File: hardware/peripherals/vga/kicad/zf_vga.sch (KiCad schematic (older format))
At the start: 33 parts

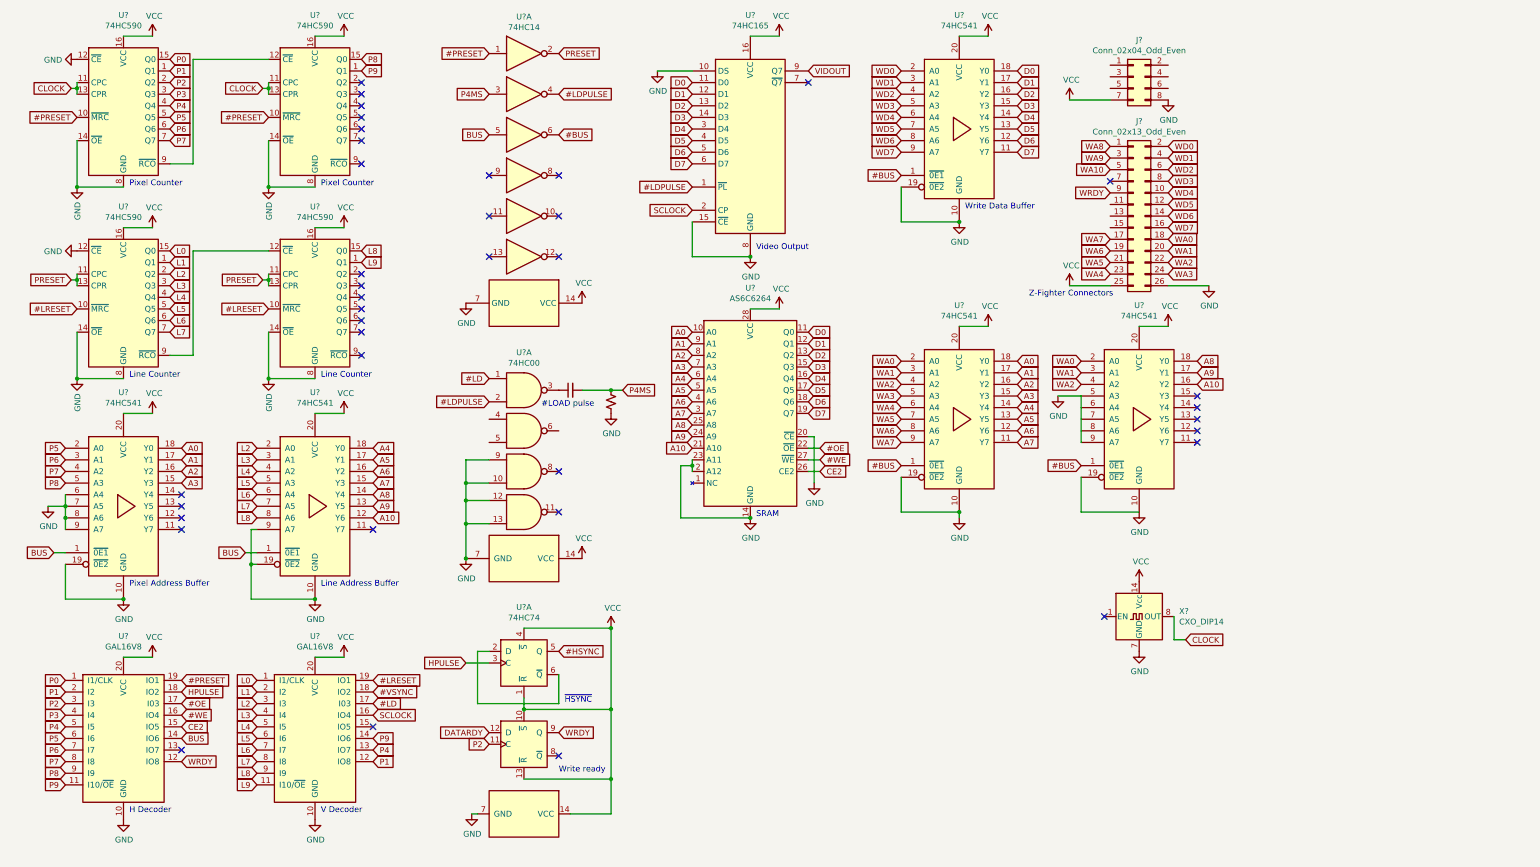
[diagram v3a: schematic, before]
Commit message: 4040 counter ICs
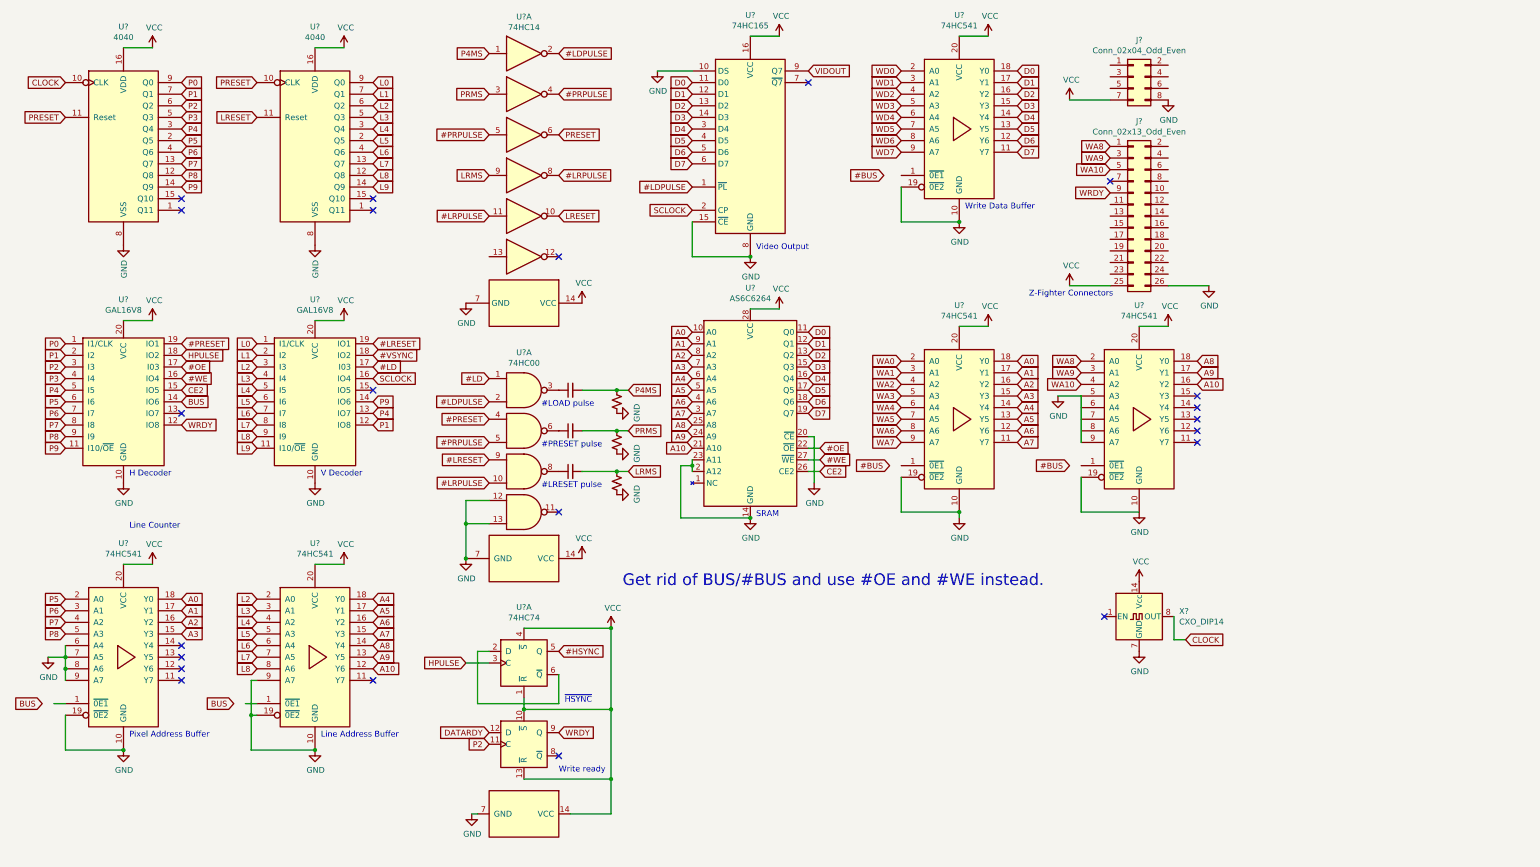
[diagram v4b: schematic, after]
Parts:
- removed U? (x4): 74HC590, symbol 74xx:74HC590
- added C? (x2): C_Small, symbol Device:C_Small
- added R? (x2): R_Small_US, symbol Device:R_Small_US
- added U? (x2): 4040, symbol 4xxx:4040
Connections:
- net #BUS: no longer U?.1 (~0E1), U?.1 (~0E1), U?.1 (~0E1), U?.6
- net #LDPULSE: now also U?.2; no longer U?.4
- net #LRESET: now also U?.9
- net #PRESET: now also U?.4; no longer U?.1
- net BUS: no longer U?.1 (~0E1), U?.1 (~0E1), U?.5
- net CLOCK: now also U?.10 (CLK)
- net GND: now also R?.1, R?.1, U?.8 (VSS), U?.8 (VSS); no longer U?.10, U?.9
- net L0: now also U?.9 (Q0)
- net L1: now also U?.7 (Q1)
- net L2: now also U?.6 (Q2)
- net L3: now also U?.5 (Q3)
- net L4: now also U?.3 (Q4)
- net L5: now also U?.2 (Q5)
- net L6: now also U?.4 (Q6)
- net L7: now also U?.13 (Q7)
- net L8: now also U?.12 (Q8)
- net L9: now also U?.14 (Q9)
- net P0: now also U?.9 (Q0)
- net P1: now also U?.7 (Q1)
- net P2: now also U?.6 (Q2)
- net P3: now also U?.5 (Q3)
- net P4: now also U?.3 (Q4)
- net P4MS: now also U?.1; no longer U?.3
- net P5: now also U?.2 (Q5)
- net P6: now also U?.4 (Q6)
- net P7: now also U?.13 (Q7)
- net P8: now also U?.12 (Q8)
- net P9: now also U?.14 (Q9)
- net PRESET: now also U?.6, U?.10 (CLK), U?.11 (Reset); no longer U?.2
- net VCC: now also U?.16 (VDD), U?.16 (VDD)
- net WA0: no longer J?.18 (Pin_18), U?.2 (A0)
- net WA1: no longer J?.20 (Pin_20), U?.3 (A1)
- net WA10: now also U?.4 (A2)
- net WA2: no longer J?.22 (Pin_22), U?.4 (A2)
- net WA3: no longer J?.24 (Pin_24)
- net WA4: no longer J?.23 (Pin_23)
- net WA5: no longer J?.21 (Pin_21)
- net WA6: no longer J?.19 (Pin_19)
- net WA7: no longer J?.17 (Pin_17)
- net WA8: now also U?.2 (A0)
- net WA9: now also U?.3 (A1)
- net WD0: no longer J?.2 (Pin_2)
- net WD1: no longer J?.4 (Pin_4)
- net WD2: no longer J?.6 (Pin_6)
- net WD3: no longer J?.8 (Pin_8)
- net WD4: no longer J?.10 (Pin_10)
- net WD5: no longer J?.12 (Pin_12)
- net WD6: no longer J?.14 (Pin_14)
- net WD7: no longer J?.16 (Pin_16)
- net #PRPULSE: now reaches U?.5
- net #PRPULSE: now also U?.4, U?.5
- net at U?.6: now also C?.1
- net #LRPULSE: now reaches U?.8
- net #LRPULSE: now also U?.10, U?.11
- net LRMS: now reaches U?.9
- net LRMS: now also C?.2, R?.2
- net at U?.8: now also C?.1
- net LRESET: now reaches U?.10
- net LRESET: now also U?.11 (Reset)
- new net PRMS: C?.2, R?.2, U?.3
- no-connect marks 38 -> 22
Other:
- note added: "#LRESET pulse"
- note added: "#PRESET pulse"
- note added: "Get rid of BUS/#BUS and use #OE and #WE instead."
- note removed: "Pixel Counter"
- moved on the sheet: U?

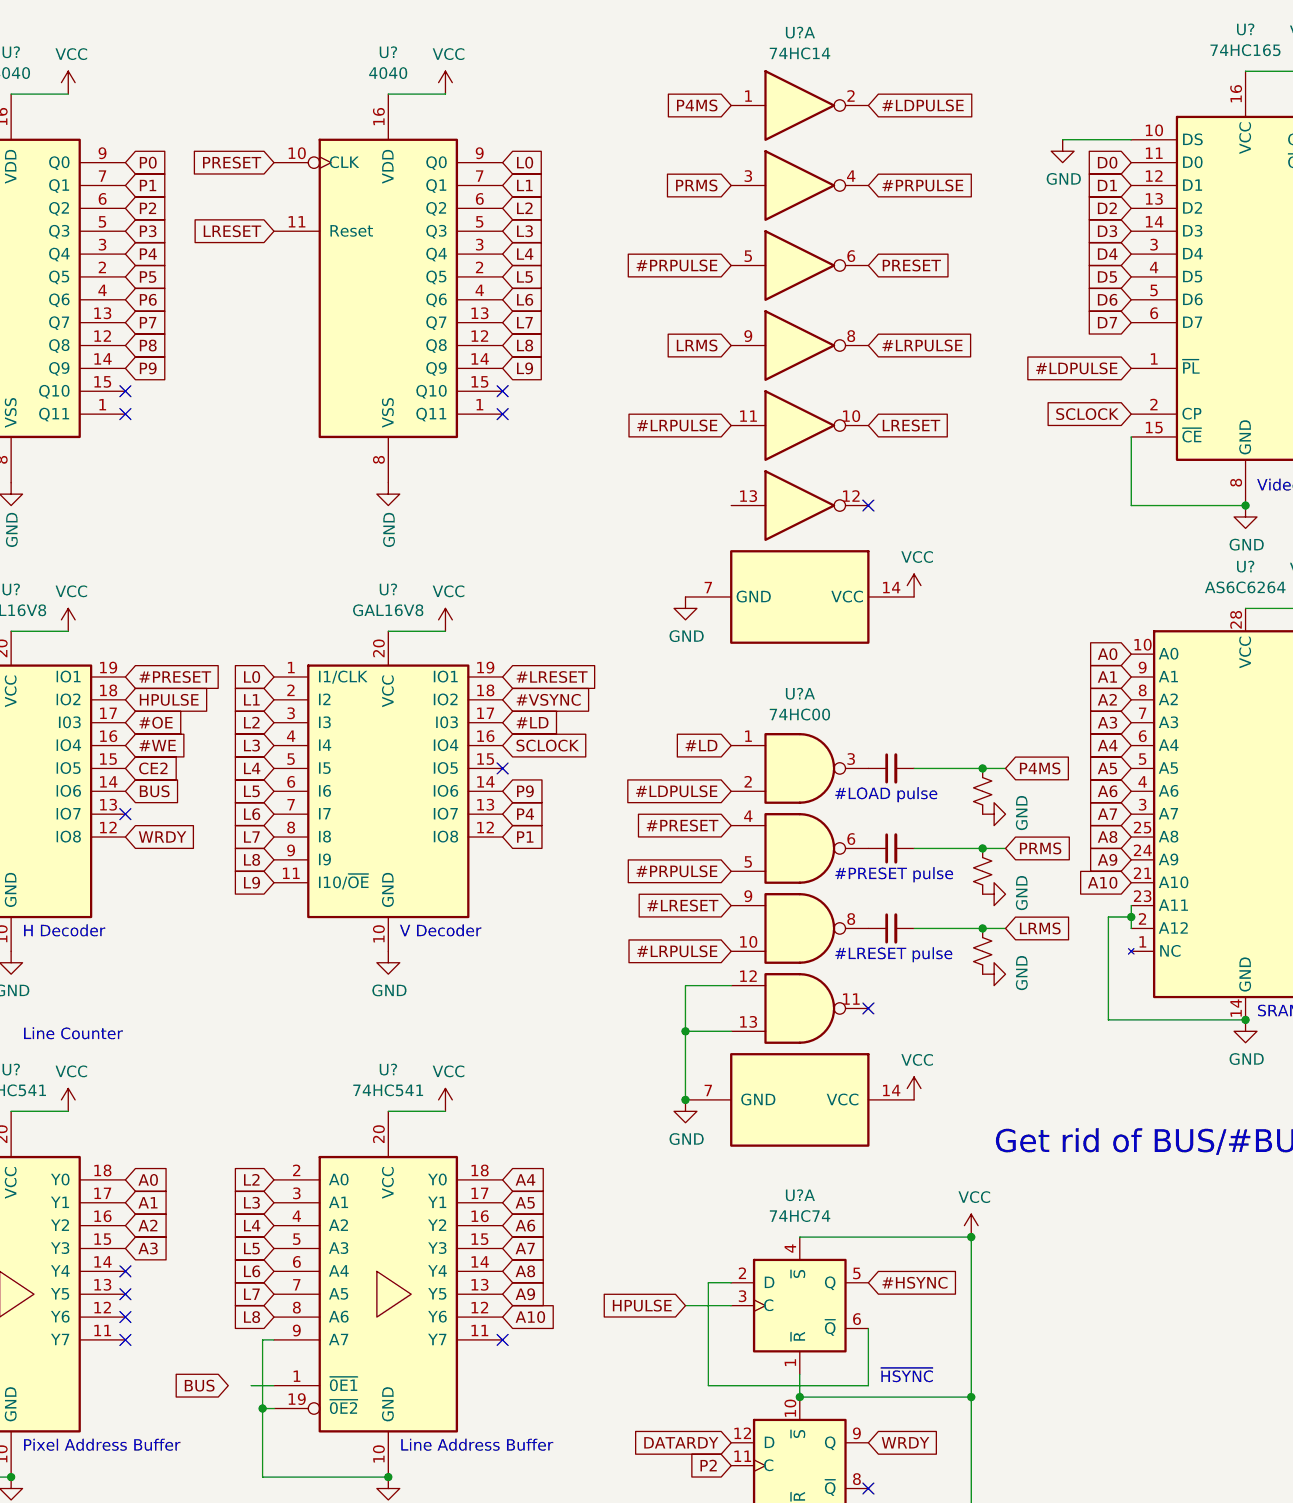
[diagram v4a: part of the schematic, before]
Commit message: Adjusted shift register load timings, synchronized pixel and line counters
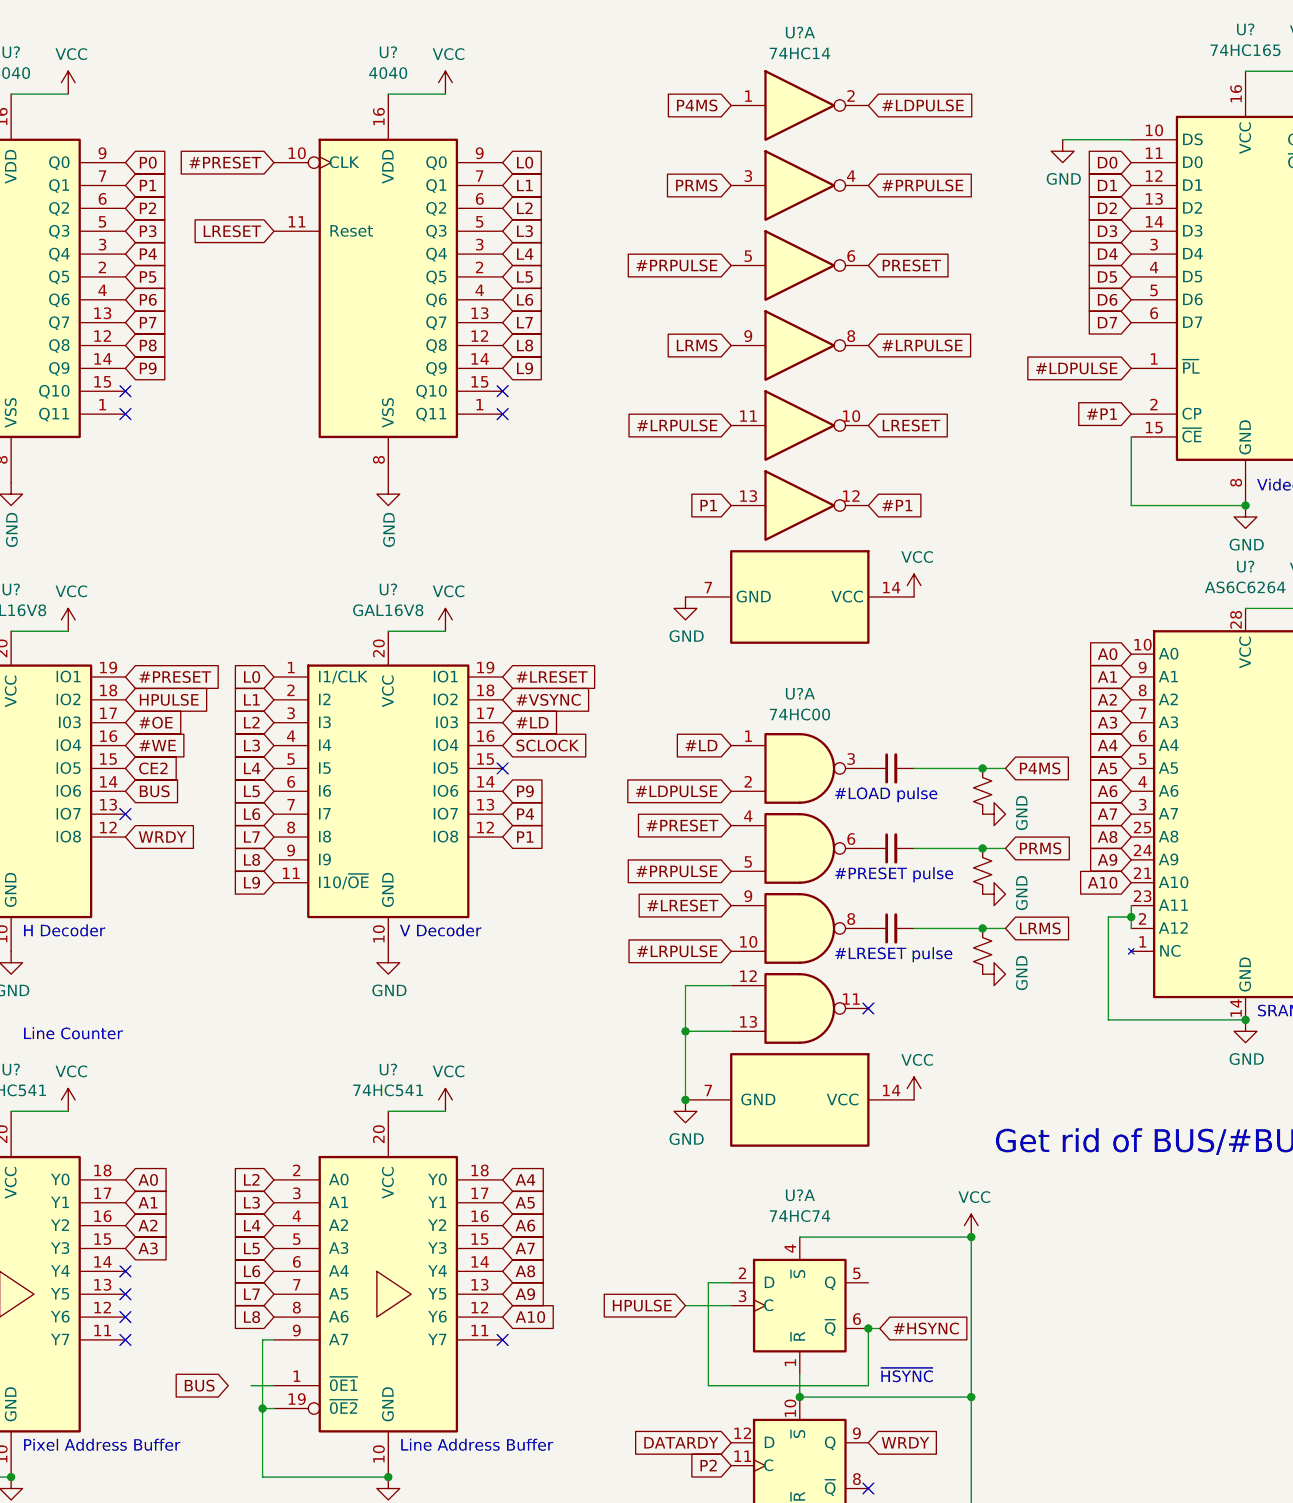
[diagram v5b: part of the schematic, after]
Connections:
- net #HSYNC: now also U?.2 (D), U?.6 (~Q); no longer U?.5 (Q)
- net #PRESET: now also U?.10 (CLK)
- net P1: now also U?.13
- net PRESET: no longer U?.10 (CLK)
- net SCLOCK: no longer U?.2 (CP)
- net #P1: now reaches U?.12
- net #P1: now also U?.2 (CP)
- no-connect marks 22 -> 21
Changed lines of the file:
@@
 Text GLabel 1950 3500 2    50   Input ~ 0
 HPULSE
-Text GLabel 6350 2250 0    50   Input ~ 0
-SCLOCK
 Text GLabel 1950 4100 2    50   Input ~ 0
 WRDY
@@
 Text Notes 5250 6500 0    50   ~ 0
 ~HSYNC
-Text GLabel 5200 6050 2    50   Input ~ 0
+Text GLabel 5250 6250 2    50   Input ~ 0
 #HSYNC
 NoConn ~ 1950 4000
@@
 	1    0    0    -1
 $EndComp
-Text GLabel 2600 1150 0    50   Input ~ 0
-PRESET
 Text GLabel 3600 1850 2    50   Input ~ 0
 L7
@@
 Text GLabel 1950 1150 2    50   Input ~ 0
 P0
-Text GLabel 4600 4400 0    50   Input ~ 0
-#LRESET
 $Comp
 L Device:R_Small_US R?
@@
 Text GLabel 4600 4050 0    50   Input ~ 0
 #PRESET
-Text Notes 5050 4300 0    50   ~ 0
-#PRESET pulse
-$Comp
-L Device:C_Small C?
-U 1 1 6235FCD8
-P 5300 4150
-F 0 "C?" V 5529 4150 50  0001 C CNN
-F 1 "C_Small" V 5437 4150 50  0001 C CNN
-F 2 "" H 5300 4150 50  0001 C CNN
-F 3 "~" H 5300 4150 50  0001 C CNN
-	1    5300 4150
-	0    -1   -1   0
-$EndComp
 Text GLabel 5800 4500 2    50   Input ~ 0
 LRMS
-Connection ~ 5700 4150
-$Comp
-L power:GND #PWR?
-U 1 1 6235FCE1
-P 5700 4350
-F 0 "#PWR?" H 5700 4100 50  0001 C CNN
-F 1 "GND" H 5705 4177 50  0000 C CNN
-F 2 "" H 5700 4350 50  0001 C CNN
-F 3 "" H 5700 4350 50  0001 C CNN
-	1    5700 4350
-	0    -1   -1   0
-$EndComp
-$Comp
-L Device:R_Small_US R?
-U 1 1 6235FCE7
-P 5700 4250
-F 0 "R?" V 5813 4250 50  0001 C CNN
-F 1 "R_Small_US" V 5814 4250 50  0001 C CNN
-F 2 "" H 5700 4250 50  0001 C CNN
-F 3 "~" H 5700 4250 50  0001 C CNN
-	1    5700 4250
-	-1   0    0    1
-$EndComp
-Wire Wire Line
-	5800 4150 5700 4150
 Text Notes 5050 4650 0    50   ~ 0
 #LRESET pulse
@@
 	0    -1   -1   0
 $EndComp
-Text GLabel 5800 4150 2    50   Input ~ 0
-PRMS
 Connection ~ 5700 4500
 $Comp
@@
 Wire Wire Line
 	5800 4500 5700 4500
-NoConn ~ 5200 2650
 Text GLabel 5200 1950 2    50   Input ~ 0
 #LRPULSE
@@
 Text GLabel 5200 2300 2    50   Input ~ 0
 LRESET
-Text GLabel 4600 4250 0    50   Input ~ 0
-#PRPULSE
 Text GLabel 4600 4600 0    50   Input ~ 0
 #LRPULSE
@@
 P4MS
 Wire Wire Line
-	5400 4150 5700 4150
-Wire Wire Line
 	5400 4500 5700 4500
 Wire Wire Line
@@
 Text Notes 5750 5500 0    100  ~ 0
 Get rid of BUS/#BUS and use #OE and #WE instead.
+Text GLabel 4600 2650 0    50   Input ~ 0
+P1
+Text GLabel 5200 2650 2    50   Input ~ 0
+#P1
+Text GLabel 6350 2250 0    50   Input ~ 0
+#P1
+Text GLabel 5800 4150 2    50   Input ~ 0
+PRMS
+Wire Wire Line
+	5800 4150 5700 4150
+$Comp
+L Device:R_Small_US R?
+U 1 1 6235FCE7
+P 5700 4250
+F 0 "R?" V 5813 4250 50  0001 C CNN
+F 1 "R_Small_US" V 5814 4250 50  0001 C CNN
+F 2 "" H 5700 4250 50  0001 C CNN
+F 3 "~" H 5700 4250 50  0001 C CNN
+	1    5700 4250
+	-1   0    0    1
+$EndComp
+$Comp
+L power:GND #PWR?
+U 1 1 6235FCE1
+P 5700 4350
+F 0 "#PWR?" H 5700 4100 50  0001 C CNN
+F 1 "GND" H 5705 4177 50  0000 C CNN
+F 2 "" H 5700 4350 50  0001 C CNN
+F 3 "" H 5700 4350 50  0001 C CNN
+	1    5700 4350
+	0    -1   -1   0
+$EndComp
+Connection ~ 5700 4150
+Wire Wire Line
+	5400 4150 5700 4150
+$Comp
+L Device:C_Small C?
+U 1 1 6235FCD8
+P 5300 4150
+F 0 "C?" V 5529 4150 50  0001 C CNN
+F 1 "C_Small" V 5437 4150 50  0001 C CNN
+F 2 "" H 5300 4150 50  0001 C CNN
+F 3 "~" H 5300 4150 50  0001 C CNN
+	1    5300 4150
+	0    -1   -1   0
+$EndComp
+Text Notes 5050 4300 0    50   ~ 0
+#PRESET pulse
+Text GLabel 2600 1150 0    50   Input ~ 0
+#PRESET
+Text GLabel 4600 4250 0    50   Input ~ 0
+#PRPULSE
+Text GLabel 4600 4400 0    50   Input ~ 0
+#LRESET
+Wire Wire Line
+	5250 6250 5200 6250
+Connection ~ 5200 6250
 $EndSCHEMATC
